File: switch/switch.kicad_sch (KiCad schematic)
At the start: 80 parts, among them U1 PI7C9X2G404SLBFDEX, U3 M24C04-WMN6TP

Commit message: WOrking.
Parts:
- removed C1, C10, C11, C14, C15, C16, C17, C19, C2, C20, C21, C22, C23, C24, C25, C26, C28, C29, C3, C30, C31, C32, C33, C4, C43, C44, C45, C46, C58, C59, C6, C60, C61, C62, C64, C65, C66, C67, C68, C69, C7, C70, C71, C8, C9: 100n, Capacitor_SMD:C_0402_1005Metric, symbol Device:C
- removed C27, C57, C63: 10u, Capacitor_SMD:C_0402_1005Metric, symbol Device:C
- removed L10, L11, L12, L13, L8, L9: MPZ1608D101BTA00, NEW:L0603, symbol NEW:MPZ1608D101BTA00
- removed R11, R12, R13, R14, R3, R4, R8, R84, R85, R86, R87: 330, Resistor_SMD:R_0402_1005Metric, symbol Device:R
- removed R15, R16, R19, R20: 5.1k, Resistor_SMD:R_0402_1005Metric, symbol Device:R
- removed R2: 1.42k, Resistor_SMD:R_0402_1005Metric, symbol Device:R
- removed R21, R5, R6, R7: 10k, Resistor_SMD:R_0402_1005Metric, symbol Device:R
- removed R22, R23, R24: 1k, Resistor_SMD:R_0402_1005Metric, symbol Device:R
- removed R88: 475, Resistor_SMD:R_0402_1005Metric, symbol Device:R
- removed U1: PI7C9X2G404SLBFDEX, NEW:LQFP-128_L14.0-W14.0-P0.40-LS16.0-BL-EP5.8, symbol NEW:PI7C9X2G404SLBFDEX
- removed U3: M24C04-WMN6TP, NEW:SOIC-8_L4.9-W3.9-P1.27-LS6.0-BL, symbol NEW:M24C04-WMN6TP
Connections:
- no-connect marks 27 -> 0
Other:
- added sheet PCIE_DOWNSTREAM (PCIE_DOWNSTREAM.kicad_sch)
- added sheet PCIE_SWITCH (PCIE_SWITCH.kicad_sch)
- added sheet PCIE_UPSTREAM (PCIE_UPSTREAM.kicad_sch)
- note removed: "EEPROM"
- note removed: "FROM RPI"
- note removed: "PORT 1"
- note removed: "PORT 2"
- note removed: "PORT 3"
- note removed: "Power Filtering"

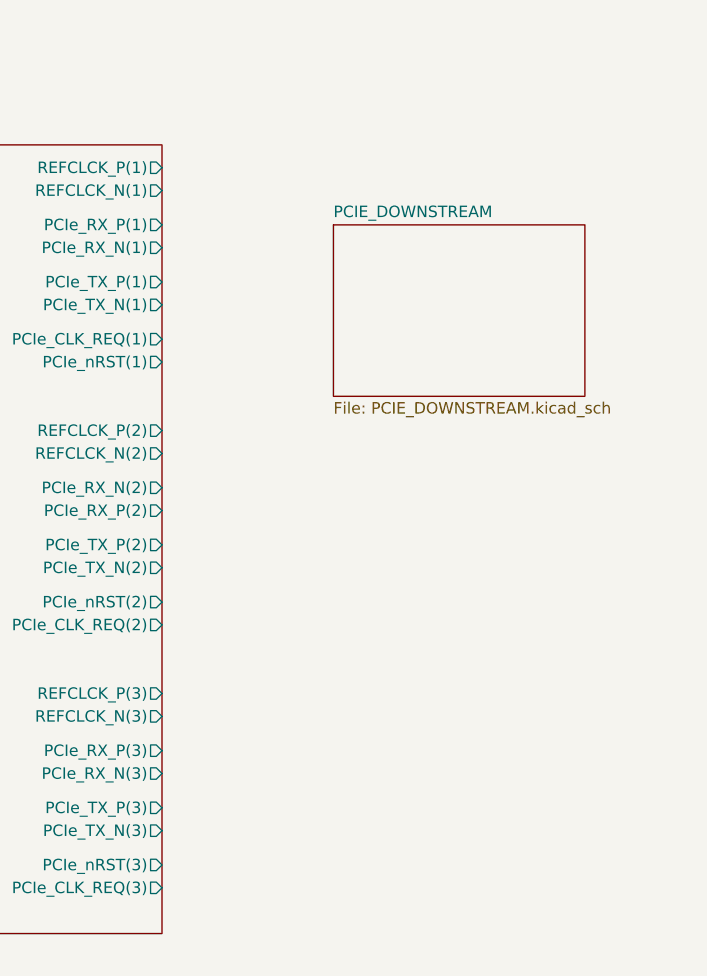
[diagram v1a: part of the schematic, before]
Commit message: Working on power supplies.
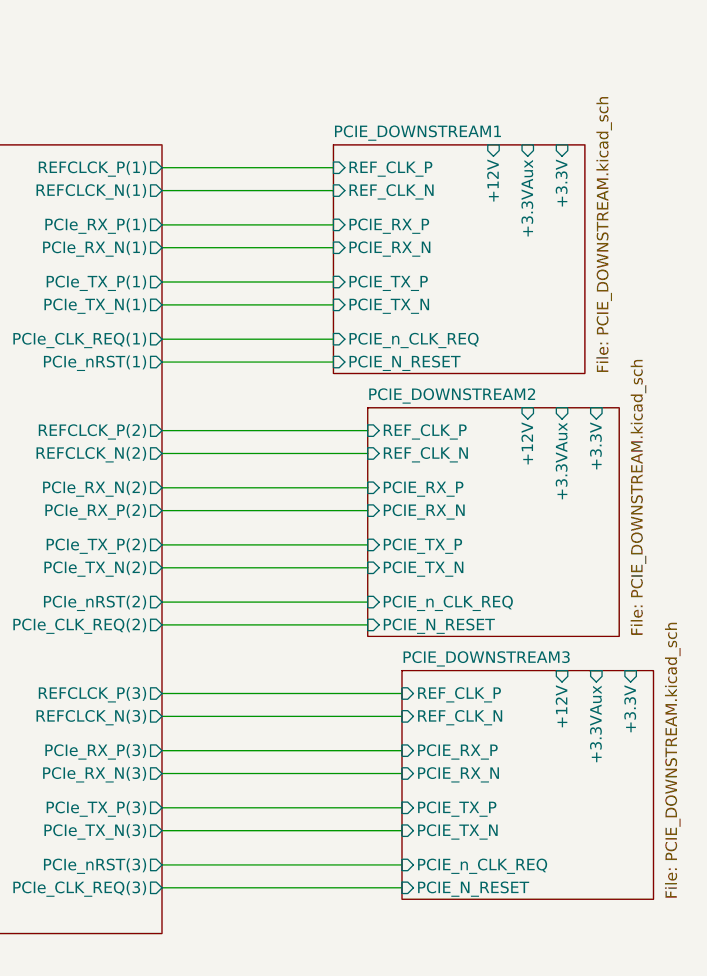
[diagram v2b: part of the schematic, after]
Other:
- sheet PCIE_DOWNSTREAM renamed PCIE_DOWNSTREAM1
- added sheet PCIE_DOWNSTREAM2 (PCIE_DOWNSTREAM.kicad_sch)
- added sheet PCIE_DOWNSTREAM3 (PCIE_DOWNSTREAM.kicad_sch)
- sheet PCIE_DOWNSTREAM1 ports: added +12V, +3.3V, +3.3VAux, PCIE_N_RESET, PCIE_RX_N, PCIE_RX_P, PCIE_TX_N, PCIE_TX_P, PCIE_n_CLK_REQ, REF_CLK_N, REF_CLK_P; removed none
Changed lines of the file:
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@@
 (kicad_sch (version 20230121) (generator eeschema)
   (paper "A3")
+  (wire (pts (xy 274.32 137.16) (xy 300.99 137.16))
+    (stroke (width 0) (type default))
+  )
+  (wire (pts (xy 274.32 107.95) (xy 297.18 107.95))
+    (stroke (width 0) (type default))
+  )
+  (wire (pts (xy 274.32 128.27) (xy 300.99 128.27))
+    (stroke (width 0) (type default))
+  )
   (wire (pts (xy 198.12 93.98) (xy 213.36 93.98))
     (stroke (width 0) (type default))
@@
     (stroke (width 0) (type default))
   )
+  (wire (pts (xy 274.32 118.11) (xy 297.18 118.11))
+    (stroke (width 0) (type default))
+  )
+  (wire (pts (xy 274.32 143.51) (xy 300.99 143.51))
+    (stroke (width 0) (type default))
+  )
+  (wire (pts (xy 274.32 101.6) (xy 297.18 101.6))
+    (stroke (width 0) (type default))
+  )
+  (wire (pts (xy 274.32 130.81) (xy 300.99 130.81))
+    (stroke (width 0) (type default))
+  )
+  (wire (pts (xy 274.32 76.2) (xy 293.37 76.2))
+    (stroke (width 0) (type default))
+  )
+  (wire (pts (xy 274.32 120.65) (xy 297.18 120.65))
+    (stroke (width 0) (type default))
+  )
   (wire (pts (xy 198.12 109.22) (xy 213.36 109.22))
     (stroke (width 0) (type default))
   )
+  (wire (pts (xy 274.32 72.39) (xy 293.37 72.39))
+    (stroke (width 0) (type default))
+  )
+  (wire (pts (xy 274.32 114.3) (xy 297.18 114.3))
+    (stroke (width 0) (type default))
+  )
+  (wire (pts (xy 274.32 69.85) (xy 293.37 69.85))
+    (stroke (width 0) (type default))
+  )
+  (wire (pts (xy 274.32 82.55) (xy 293.37 82.55))
+    (stroke (width 0) (type default))
+  )
+  (wire (pts (xy 274.32 147.32) (xy 300.99 147.32))
+    (stroke (width 0) (type default))
+  )
   (wire (pts (xy 198.12 102.87) (xy 213.36 102.87))
     (stroke (width 0) (type default))
   )
+  (wire (pts (xy 274.32 99.06) (xy 297.18 99.06))
+    (stroke (width 0) (type default))
+  )
+  (wire (pts (xy 274.32 88.9) (xy 293.37 88.9))
+    (stroke (width 0) (type default))
+  )
+  (wire (pts (xy 274.32 85.09) (xy 293.37 85.09))
+    (stroke (width 0) (type default))
+  )
+  (wire (pts (xy 274.32 78.74) (xy 293.37 78.74))
+    (stroke (width 0) (type default))
+  )
   (wire (pts (xy 198.12 87.63) (xy 213.36 87.63))
     (stroke (width 0) (type default))
   )
+  (wire (pts (xy 274.32 149.86) (xy 300.99 149.86))
+    (stroke (width 0) (type default))
+  )
+  (wire (pts (xy 274.32 91.44) (xy 293.37 91.44))
+    (stroke (width 0) (type default))
+  )
   (wire (pts (xy 198.12 100.33) (xy 213.36 100.33))
     (stroke (width 0) (type default))
   )
+  (wire (pts (xy 274.32 140.97) (xy 300.99 140.97))
+    (stroke (width 0) (type default))
+  )
+  (wire (pts (xy 274.32 111.76) (xy 297.18 111.76))
+    (stroke (width 0) (type default))
+  )
   (wire (pts (xy 198.12 90.17) (xy 213.36 90.17))
     (stroke (width 0) (type default))
+  )
+  (wire (pts (xy 274.32 105.41) (xy 297.18 105.41))
+    (stroke (width 0) (type default))
+  )
+  (wire (pts (xy 274.32 134.62) (xy 300.99 134.62))
+    (stroke (width 0) (type default))
+  )
+  (sheet (at 297.18 96.52) (size 27.94 25.4)
+    (stroke (width 0.1524) (type solid))
+    (fill (color 0 0 0 0.0000))
+    (property "Sheetname" "PCIE_DOWNSTREAM2" (at 297.18 95.8084 0)
+      (effects (font (size 1.27 1.27)) (justify left bottom))
+    )
+    (property "Sheetfile" "PCIE_DOWNSTREAM.kicad_sch" (at 326.39 121.92 90)
+      (effects (font (size 1.27 1.27)) (justify left top))
+    )
+    (pin "PCIE_TX_N" input (at 297.18 114.3 180)
+      (effects (font (size 1.27 1.27)) (justify left))
+    )
+    (pin "PCIE_TX_P" input (at 297.18 111.76 180)
+      (effects (font (size 1.27 1.27)) (justify left))
+    )
+    (pin "+3.3V" input (at 322.58 96.52 90)
+      (effects (font (size 1.27 1.27)) (justify right))
+    )
+    (pin "+3.3VAux" input (at 318.77 96.52 90)
+      (effects (font (size 1.27 1.27)) (justify right))
+    )
+    (pin "PCIE_n_CLK_REQ" input (at 297.18 118.11 180)
+      (effects (font (size 1.27 1.27)) (justify left))
+    )
+    (pin "+12V" input (at 314.96 96.52 90)
+      (effects (font (size 1.27 1.27)) (justify right))
+    )
+    (pin "PCIE_N_RESET" input (at 297.18 120.65 180)
+      (effects (font (size 1.27 1.27)) (justify left))
+    )
+    (pin "REF_CLK_P" input (at 297.18 99.06 180)
+      (effects (font (size 1.27 1.27)) (justify left))
+    )
+    (pin "REF_CLK_N" input (at 297.18 101.6 180)
+      (effects (font (size 1.27 1.27)) (justify left))
+    )
+    (pin "PCIE_RX_P" input (at 297.18 105.41 180)
+      (effects (font (size 1.27 1.27)) (justify left))
+    )
+    (pin "PCIE_RX_N" input (at 297.18 107.95 180)
+      (effects (font (size 1.27 1.27)) (justify left))
+    )
+    (instances
+      (project "switch"
+        (path "/bb24befe-87e3-4bdd-b50d-d3887bf8bcae" (page "5"))
+      )
+    )
   )
   (sheet (at 213.36 67.31) (size 60.96 87.63) (fields_autoplaced)
@@
     )
   )
-  (sheet (at 293.37 76.2) (size 27.94 19.05) (fields_autoplaced)
+  (sheet (at 300.99 125.73) (size 27.94 25.4)
     (stroke (width 0.1524) (type solid))
     (fill (color 0 0 0 0.0000))
-    (property "Sheetname" "PCIE_DOWNSTREAM" (at 293.37 75.4884 0)
+    (property "Sheetname" "PCIE_DOWNSTREAM3" (at 300.99 125.0184 0)
       (effects (font (size 1.27 1.27)) (justify left bottom))
     )
-    (property "Sheetfile" "PCIE_DOWNSTREAM.kicad_sch" (at 293.37 95.8346 0)
+    (property "Sheetfile" "PCIE_DOWNSTREAM.kicad_sch" (at 330.2 151.13 90)
       (effects (font (size 1.27 1.27)) (justify left top))
     )
+    (pin "PCIE_TX_N" input (at 300.99 143.51 180)
+      (effects (font (size 1.27 1.27)) (justify left))
+    )
+    (pin "PCIE_TX_P" input (at 300.99 140.97 180)
+      (effects (font (size 1.27 1.27)) (justify left))
+    )
+    (pin "+3.3V" input (at 326.39 125.73 90)
+      (effects (font (size 1.27 1.27)) (justify right))
+    )
+    (pin "+3.3VAux" input (at 322.58 125.73 90)
+      (effects (font (size 1.27 1.27)) (justify right))
+    )
+    (pin "PCIE_n_CLK_REQ" input (at 300.99 147.32 180)
+      (effects (font (size 1.27 1.27)) (justify left))
+    )
+    (pin "+12V" input (at 318.77 125.73 90)
+      (effects (font (size 1.27 1.27)) (justify right))
+    )
+    (pin "PCIE_N_RESET" input (at 300.99 149.86 180)
+      (effects (font (size 1.27 1.27)) (justify left))
+    )
+    (pin "REF_CLK_P" input (at 300.99 128.27 180)
+      (effects (font (size 1.27 1.27)) (justify left))
+    )
+    (pin "REF_CLK_N" input (at 300.99 130.81 180)
+      (effects (font (size 1.27 1.27)) (justify left))
+    )
+    (pin "PCIE_RX_P" input (at 300.99 134.62 180)
+      (effects (font (size 1.27 1.27)) (justify left))
+    )
+    (pin "PCIE_RX_N" input (at 300.99 137.16 180)
+      (effects (font (size 1.27 1.27)) (justify left))
+    )
     (instances
+      (project "switch"
+        (path "/bb24befe-87e3-4bdd-b50d-d3887bf8bcae" (page "6"))
+      )
+    )
+  )
+  (sheet (at 293.37 67.31) (size 27.94 25.4)
+    (stroke (width 0.1524) (type solid))
+    (fill (color 0 0 0 0.0000))
+    (property "Sheetname" "PCIE_DOWNSTREAM1" (at 293.37 66.5984 0)
+      (effects (font (size 1.27 1.27)) (justify left bottom))
+    )
+    (property "Sheetfile" "PCIE_DOWNSTREAM.kicad_sch" (at 322.58 92.71 90)
+      (effects (font (size 1.27 1.27)) (justify left top))
+    )
+    (pin "PCIE_TX_N" input (at 293.37 85.09 180)
+      (effects (font (size 1.27 1.27)) (justify left))
+    )
+    (pin "PCIE_TX_P" input (at 293.37 82.55 180)
+      (effects (font (size 1.27 1.27)) (justify left))
+    )
+    (pin "+3.3V" input (at 318.77 67.31 90)
+      (effects (font (size 1.27 1.27)) (justify right))
+    )
+    (pin "+3.3VAux" input (at 314.96 67.31 90)
+      (effects (font (size 1.27 1.27)) (justify right))
+    )
+    (pin "PCIE_n_CLK_REQ" input (at 293.37 88.9 180)
+      (effects (font (size 1.27 1.27)) (justify left))
+    )
+    (pin "+12V" input (at 311.15 67.31 90)
+      (effects (font (size 1.27 1.27)) (justify right))
+    )
+    (pin "PCIE_N_RESET" input (at 293.37 91.44 180)
+      (effects (font (size 1.27 1.27)) (justify left))
+    )
+    (pin "REF_CLK_P" input (at 293.37 69.85 180)
+      (effects (font (size 1.27 1.27)) (justify left))
+    )
+    (pin "REF_CLK_N" input (at 293.37 72.39 180)
+      (effects (font (size 1.27 1.27)) (justify left))
+    )
+    (pin "PCIE_RX_P" input (at 293.37 76.2 180)
+      (effects (font (size 1.27 1.27)) (justify left))
+    )
+    (pin "PCIE_RX_N" input (at 293.37 78.74 180)
+      (effects (font (size 1.27 1.27)) (justify left))
+    )
+    (instances

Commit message: Finished with Schematic.
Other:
- added sheet SW_PSU (SW_PSU.kicad_sch)
